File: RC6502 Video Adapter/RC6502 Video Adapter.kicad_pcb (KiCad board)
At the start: 2 copper layers, 99.1 x 66 mm, 19 parts, among them J1 CONN_01X39, J2 CONN_02X20, J3 Video, J4 FTDI, J5 ICSP, U1 ATMEGA328P-PU, Y1 16 Mhz

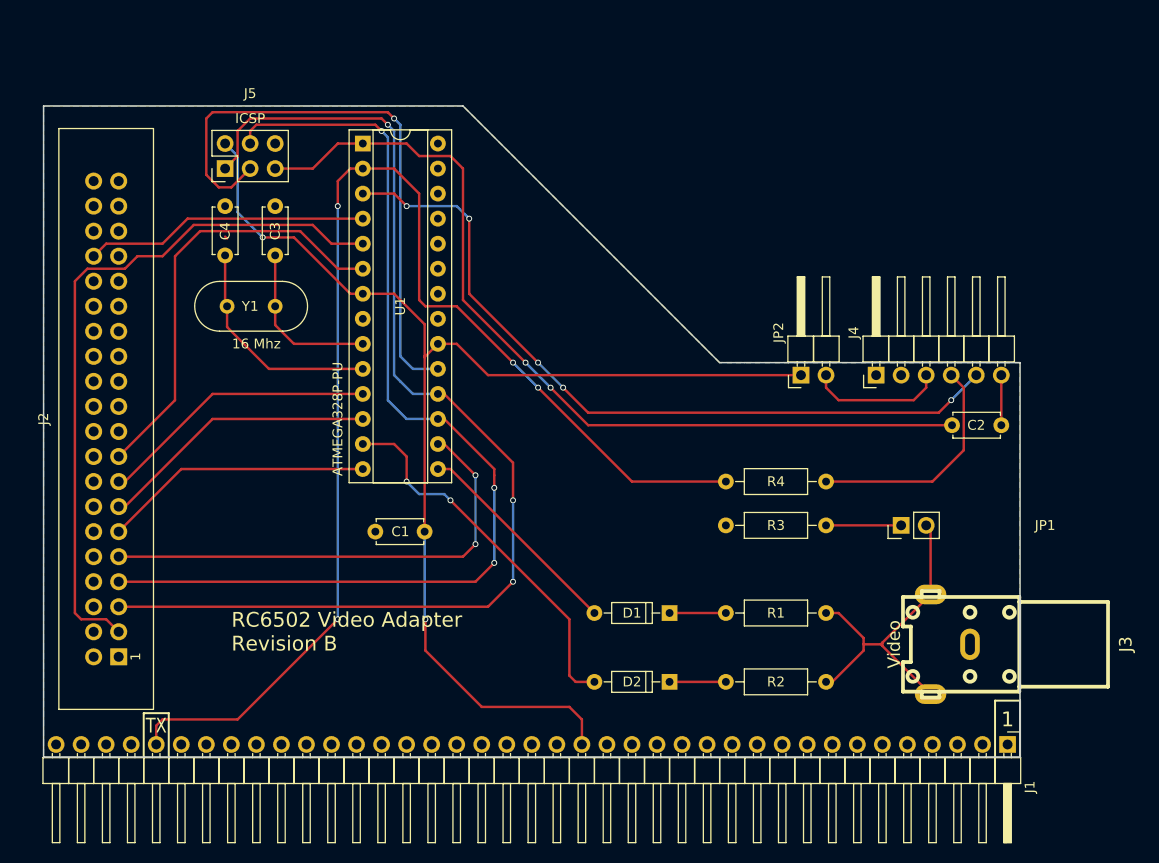
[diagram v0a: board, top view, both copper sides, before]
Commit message: Video Adapter revision B
Adds IO expanders for possibly offloading the actual image output rendering to an analog module via a separate connector.
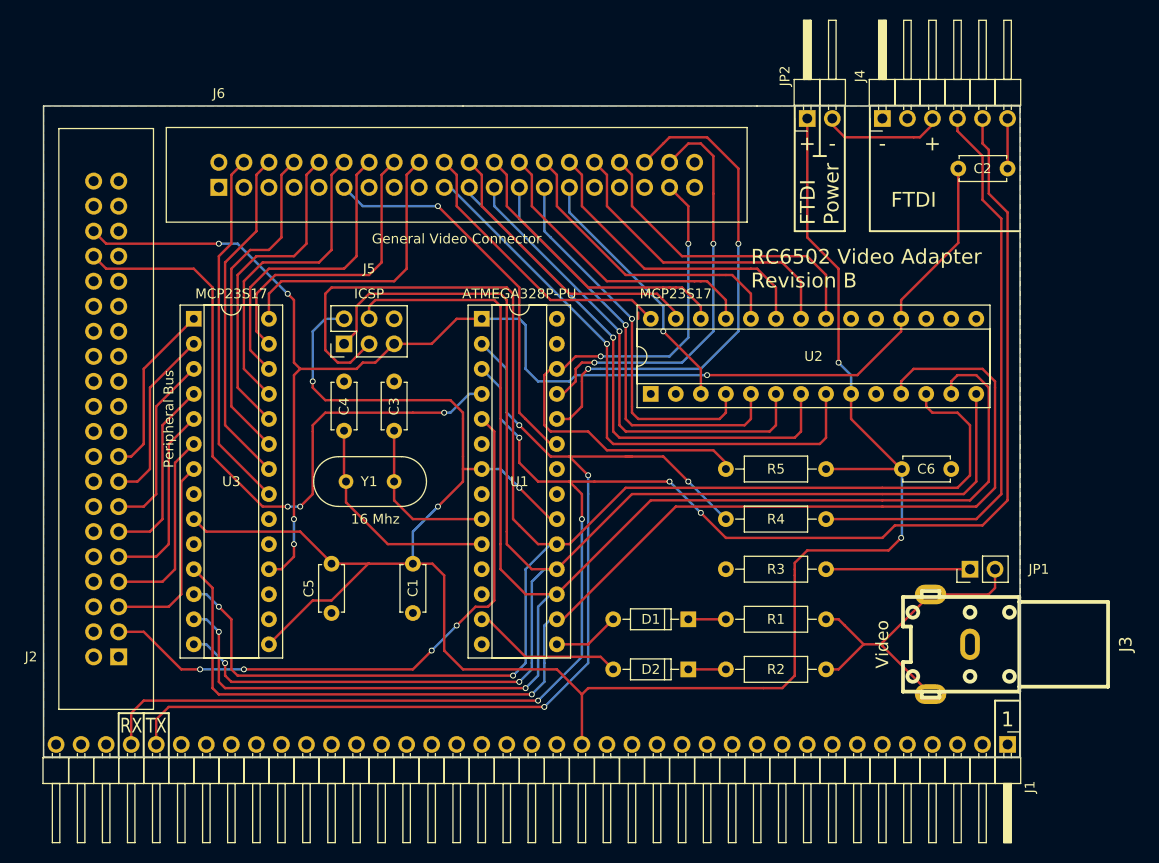
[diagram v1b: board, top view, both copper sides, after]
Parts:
- added C5: 100nF, Capacitors_THT:C_Disc_D4.7mm_W2.5mm_P5.00mm, F.Cu at (145.4, 132.7)
- added C6: 100nF, Capacitors_THT:C_Disc_D4.7mm_W2.5mm_P5.00mm, F.Cu at (208.3, 118.1)
- added J6: General Video Connector, Connectors:IDC_Header_Straight_40pins, F.Cu at (134.0, 89.5)
- added R5: 10k, Resistors_THT:R_Axial_DIN0207_L6.3mm_D2.5mm_P10.16mm_Horizontal, F.Cu at (185.4, 118.1)
- added U2: MCP23S17, Housings_DIP:DIP-28_W7.62mm_Socket, F.Cu at (177.8, 110.5)
- added U3: MCP23S17, Housings_DIP:DIP-28_W7.62mm_Socket, F.Cu at (131.4, 102.9)
- J2: value CONN_02X20 -> Peripheral Bus
- moved C2 26.0 mm to (214.0, 87.6)
- moved J4 26.0 mm to (201.3, 82.5)
- moved JP2 26.0 mm to (193.7, 82.5)
- moved C3 21.5 mm to (151.8, 109.2)
- moved C4 21.5 mm to (146.7, 109.2)
- moved J5 21.5 mm to (146.7, 105.4)
- moved U1 21.5 mm to (160.7, 102.9)
- moved Y1 21.5 mm to (151.8, 119.4)
- moved C1 9.09 mm to (153.7, 132.7), turned to 90 degrees
- moved JP1 8.28 mm to (210.2, 128.3)
- moved R3 4.45 mm to (185.4, 128.3)
- moved R4 3.81 mm to (195.6, 123.2)
- moved D2 2.29 mm to (181.6, 138.4)
- moved D1 2.01 mm to (181.6, 133.3)
- moved R2 1.27 mm to (195.6, 138.4)
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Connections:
- net Net-(J5-Pad3) renamed SCK
- C2 pad 2: RESET -> P_RESET
- J1 pad 36: (no net) -> RX
- J2 pad 36: (no net) -> P_RESET
- J4 pad 5: Net-(J4-Pad5) -> RX
- J5 pad 1: OUT_D6 -> MISO
- J5 pad 4: OUT_D5 -> MOSI
- J5 pad 5: RESET -> P_RESET
- U1 pad 1: RESET -> P_RESET
- U1 pad 11: OUT_D1 -> (no net)
- U1 pad 12: OUT_D2 -> (no net)
- U1 pad 14: OUT_D3 -> (no net)
- U1 pad 16: OUT_D4 -> SS
- U1 pad 17: OUT_D5 -> MOSI
- U1 pad 18: OUT_D6 -> MISO
- U1 pad 23: (no net) -> GV_CS
- U1 pad 24: (no net) -> GV_RW
- U1 pad 25: (no net) -> GV_E
- U1 pad 26: (no net) -> GV_DETECT
- U1 pad 3: Net-(J4-Pad5) -> RX
- U1 pad 6: OUT_D0 -> (no net)
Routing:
- net RX: track 0.00 -> 174.7 mm, vias 0 -> 5
- net MOSI: track 0.00 -> 163.2 mm, vias 0 -> 2
- net MISO: track 0.00 -> 155.5 mm, vias 0 -> 2
- net P_RESET: track 0.00 -> 142.2 mm, vias 0 -> 5
- net SS: track 0.00 -> 127.8 mm, vias 0 -> 1
- net SCK: track 59.8 -> 170.8 mm, vias 1 -> 2
- net VCC: track 125.8 -> 224.7 mm, vias 2 -> 5
- net OUT_D6: track 114.9 -> 20.1 mm, vias 3 -> 0
- net RESET: track 89.4 -> 0.00 mm, vias 2 -> 0
- net OUT_D5: track 104.8 -> 19.7 mm, vias 3 -> 0
- net Net-(J4-Pad5): track 77.5 -> 0.00 mm, vias 5 -> 0
- net GV_A8: track 0.00 -> 59.8 mm, vias 0 -> 1
- net GV_DETECT: track 0.00 -> 58.6 mm, vias 0 -> 2
- net GV_A9: track 0.00 -> 54.2 mm, vias 0 -> 1
- net GV_RW: track 0.00 -> 52.4 mm, vias 0 -> 2
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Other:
- outline, holes or cut-outs redrawn
- board text added: "+"
- board text added: "-"
- board text added: "FTDI"
- board text added: "FTDI Power"
- board text added: "RX"

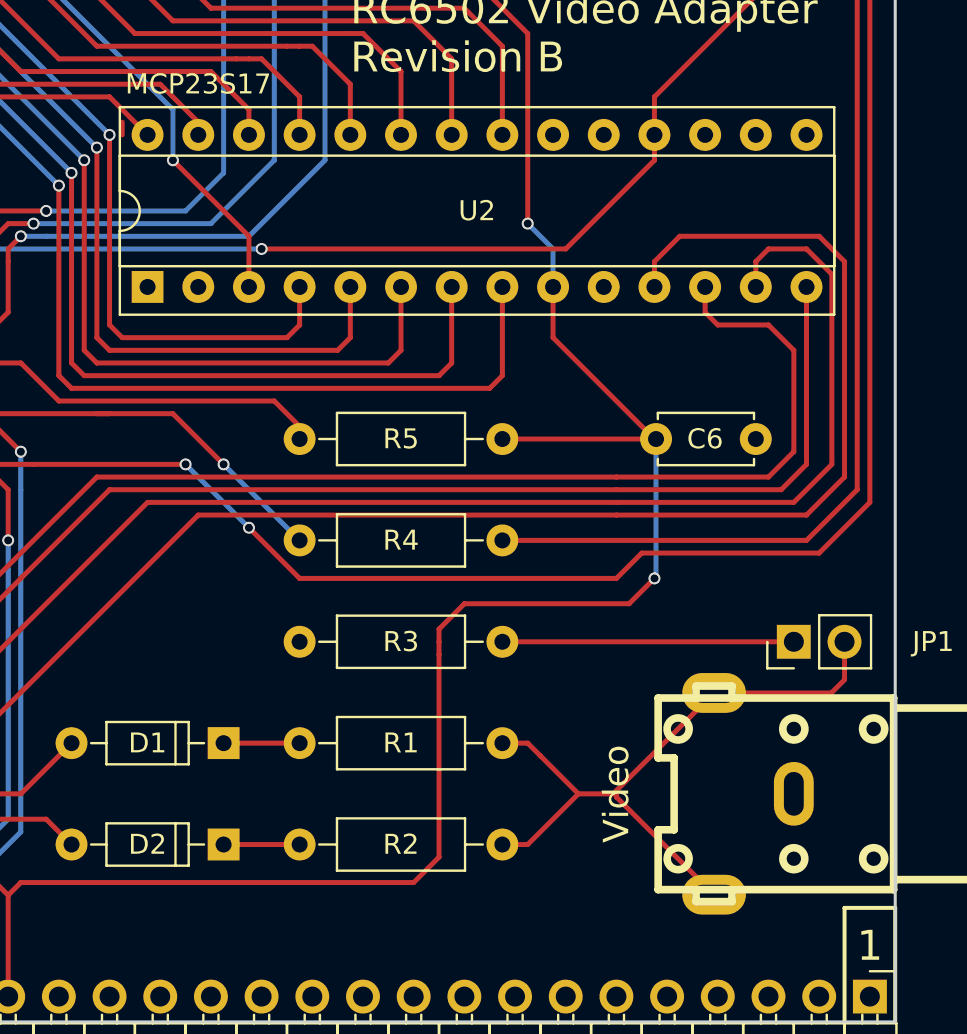
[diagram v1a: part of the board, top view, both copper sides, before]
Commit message: Fixed video adapter rca connector footprint.
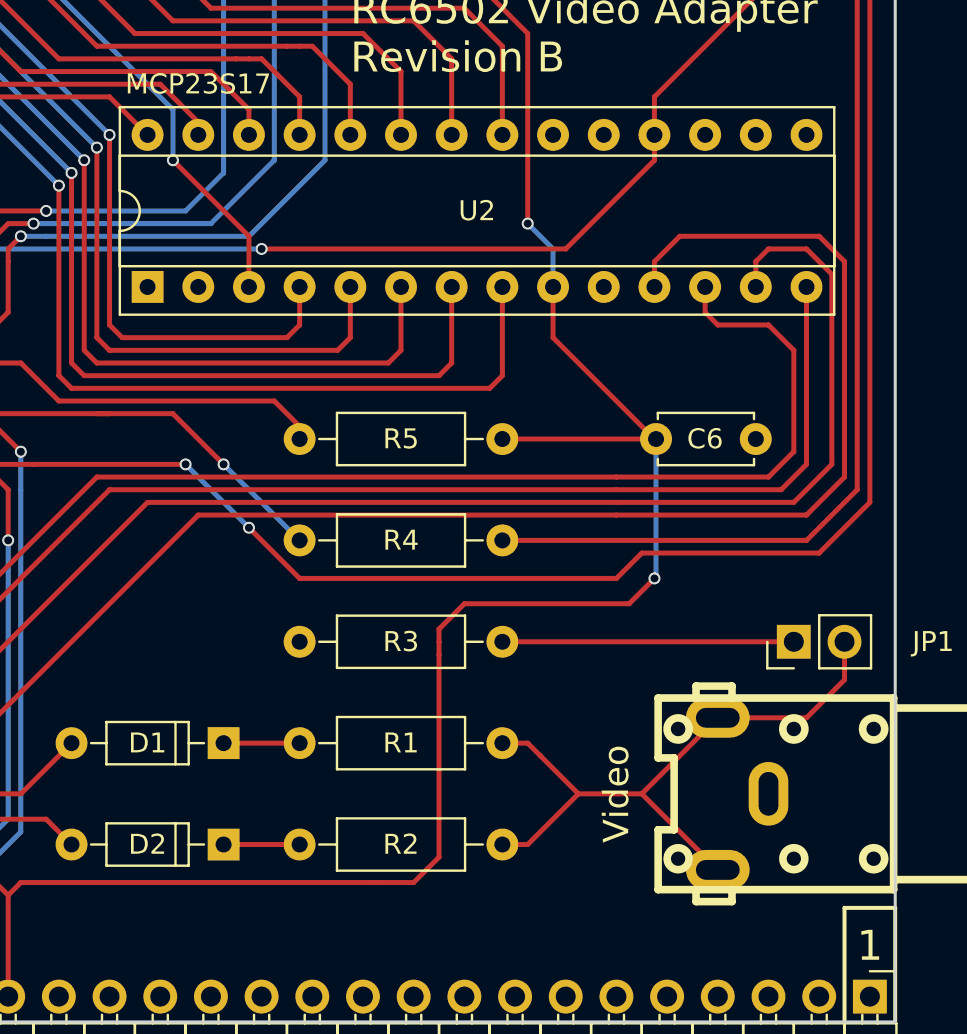
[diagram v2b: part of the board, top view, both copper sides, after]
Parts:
- J3: footprint w_conn_av:rca_yellow -> rca:rca_yellow
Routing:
- net Net-(J3-Pad2): track 34.6 -> 32.7 mm
- net (no net): track 0.64 -> 0.00 mm
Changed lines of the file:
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@@
     (thickness 1.6)
     (drawings 31)
-    (tracks 600)
+    (tracks 598)
     (zones 0)
     (modules 25)
@@
     (34 B.Paste user)
     (35 F.Paste user)
-    (36 B.SilkS user)
+    (36 B.SilkS user hide)
     (37 F.SilkS user)
     (38 B.Mask user)
@@
       (net 1 GND))
   )
-  (module w_conn_av:rca_yellow (layer F.Cu)
-    (at 210.185 135.89 90)
-    (descr "RCA Audio connector, yellow, Pro Signal p/n PSG01547")
-    (tags "rca, audio")
-    (fp_text reference J3 (at 0 15.7988 90) (layer F.SilkS)
-      (effects (font (thickness 0.3048)))
-    )
-    (fp_text value Video (at 0 -8.89 90) (layer F.SilkS)
-      (effects (font (thickness 0.3048)))
-    )
-    (fp_circle (center -3.2512 -5.79882) (end -3.79984 -5.79882) (layer F.SilkS) (width 0.381))
-    (fp_circle (center 3.2512 -5.79882) (end 2.70002 -5.84962) (layer F.SilkS) (width 0.381))
-    (fp_circle (center 3.2512 4.0005) (end 2.70002 4.04876) (layer F.SilkS) (width 0.381))
-    (fp_circle (center -3.2512 4.0005) (end -3.79984 3.9497) (layer F.SilkS) (width 0.381))
-    (fp_circle (center -3.2512 0) (end -3.79984 0) (layer F.SilkS) (width 0.381))
-    (fp_circle (center 3.2512 0) (end 2.70002 -0.0508) (layer F.SilkS) (width 0.381))
-    (fp_line (start -4.30022 5.00126) (end -4.30022 14.00048) (layer F.SilkS) (width 0.381))
-    (fp_line (start -4.30022 14.00048) (end 4.30022 14.00048) (layer F.SilkS) (width 0.381))
-    (fp_line (start 4.30022 14.00048) (end 4.30022 5.00126) (layer F.SilkS) (width 0.381))
-    (fp_line (start 4.8006 -4.89966) (end 5.40004 -4.89966) (layer F.SilkS) (width 0.381))
-    (fp_line (start 5.40004 -4.89966) (end 5.40004 -3.0988) (layer F.SilkS) (width 0.381))
-    (fp_line (start 5.40004 -3.0988) (end 4.8006 -3.0988) (layer F.SilkS) (width 0.381))
-    (fp_line (start -5.40004 -4.89966) (end -4.8006 -4.89966) (layer F.SilkS) (width 0.381))
-    (fp_line (start -4.8006 -3.0988) (end -5.40004 -3.0988) (layer F.SilkS) (width 0.381))
-    (fp_line (start -5.40004 -3.0988) (end -5.40004 -4.89966) (layer F.SilkS) (width 0.381))
-    (fp_line (start -4.8006 -6.79958) (end -1.80086 -6.79958) (layer F.SilkS) (width 0.381))
-    (fp_line (start -1.80086 -6.79958) (end -1.80086 -5.99948) (layer F.SilkS) (width 0.381))
-    (fp_line (start -1.80086 -5.99948) (end 1.80086 -5.99948) (layer F.SilkS) (width 0.381))
-    (fp_line (start 1.80086 -5.99948) (end 1.80086 -6.79958) (layer F.SilkS) (width 0.381))
-    (fp_line (start 1.80086 -6.79958) (end 4.8006 -6.79958) (layer F.SilkS) (width 0.381))
-    (fp_line (start 4.8006 5.00126) (end -4.8006 5.00126) (layer F.SilkS) (width 0.381))
-    (fp_line (start -4.8006 4.99872) (end -4.8006 -6.80212) (layer F.SilkS) (width 0.381))
-    (fp_line (start 4.8006 -6.79958) (end 4.8006 5.00126) (layer F.SilkS) (width 0.381))
-    (pad 2 thru_hole oval (at 5.0546 -3.99796 90) (size 1.99898 3.19786) (drill oval 0.99568 2.1971) (layers *.Cu *.Mask F.SilkS)
-      (net 15 "Net-(J3-Pad2)"))
-    (pad 1 thru_hole oval (at 0 0 90) (size 3.19786 1.99898) (drill oval 2.1971 0.99568) (layers *.Cu *.Mask F.SilkS)
-      (net 1 GND))
-    (pad 2 thru_hole oval (at -5.0546 -3.99796 90) (size 1.99898 3.19786) (drill oval 0.99568 2.1971) (layers *.Cu *.Mask F.SilkS)
-      (net 15 "Net-(J3-Pad2)"))
-    (model walter/conn_av/rca_yellow.wrl
-      (at (xyz 0 0 0))
-      (scale (xyz 1 1 1))
-      (rotate (xyz 0 0 0))
-    )
-  )
   (module Pin_Headers:Pin_Header_Angled_1x06_Pitch2.54mm (layer F.Cu)
     (at 201.295 82.55 90)
@@
     )
   )
+  (module rca:rca_yellow (layer F.Cu)
+    (at 210.185 135.89 90)
+    (descr "RCA Audio connector, yellow, Pro Signal p/n PSG01547")
+    (tags "rca, audio")
+    (fp_text reference J3 (at 0 15.7988 90) (layer F.SilkS)
+      (effects (font (thickness 0.3048)))
+    )
+    (fp_text value Video (at 0 -8.89 90) (layer F.SilkS)
+      (effects (font (thickness 0.3048)))
+    )
+    (fp_circle (center -3.2512 -5.79882) (end -3.79984 -5.79882) (layer F.SilkS) (width 0.381))
+    (fp_circle (center 3.2512 -5.79882) (end 2.70002 -5.84962) (layer F.SilkS) (width 0.381))
+    (fp_circle (center 3.2512 4.0005) (end 2.70002 4.04876) (layer F.SilkS) (width 0.381))
+    (fp_circle (center -3.2512 4.0005) (end -3.79984 3.9497) (layer F.SilkS) (width 0.381))
+    (fp_circle (center -3.2512 0) (end -3.79984 0) (layer F.SilkS) (width 0.381))
+    (fp_circle (center 3.2512 0) (end 2.70002 -0.0508) (layer F.SilkS) (width 0.381))
+    (fp_line (start -4.30022 5.00126) (end -4.30022 14.00048) (layer F.SilkS) (width 0.381))
+    (fp_line (start -4.30022 14.00048) (end 4.30022 14.00048) (layer F.SilkS) (width 0.381))
+    (fp_line (start 4.30022 14.00048) (end 4.30022 5.00126) (layer F.SilkS) (width 0.381))
+    (fp_line (start 4.8006 -4.89966) (end 5.40004 -4.89966) (layer F.SilkS) (width 0.381))
+    (fp_line (start 5.40004 -4.89966) (end 5.40004 -3.0988) (layer F.SilkS) (width 0.381))
+    (fp_line (start 5.40004 -3.0988) (end 4.8006 -3.0988) (layer F.SilkS) (width 0.381))
+    (fp_line (start -5.40004 -4.89966) (end -4.8006 -4.89966) (layer F.SilkS) (width 0.381))
+    (fp_line (start -4.8006 -3.0988) (end -5.40004 -3.0988) (layer F.SilkS) (width 0.381))
+    (fp_line (start -5.40004 -3.0988) (end -5.40004 -4.89966) (layer F.SilkS) (width 0.381))
+    (fp_line (start -4.8006 -6.79958) (end -1.80086 -6.79958) (layer F.SilkS) (width 0.381))
+    (fp_line (start -1.80086 -6.79958) (end -1.80086 -5.99948) (layer F.SilkS) (width 0.381))
+    (fp_line (start -1.80086 -5.99948) (end 1.80086 -5.99948) (layer F.SilkS) (width 0.381))
+    (fp_line (start 1.80086 -5.99948) (end 1.80086 -6.79958) (layer F.SilkS) (width 0.381))
+    (fp_line (start 1.80086 -6.79958) (end 4.8006 -6.79958) (layer F.SilkS) (width 0.381))
+    (fp_line (start 4.8006 5.00126) (end -4.8006 5.00126) (layer F.SilkS) (width 0.381))
+    (fp_line (start -4.8006 4.99872) (end -4.8006 -6.80212) (layer F.SilkS) (width 0.381))
+    (fp_line (start 4.8006 -6.79958) (end 4.8006 5.00126) (layer F.SilkS) (width 0.381))
+    (pad 2 thru_hole oval (at 3.81 -3.81 90) (size 1.99898 3.19786) (drill oval 0.99568 2.1971) (layers *.Cu *.Mask F.SilkS)
+      (net 15 "Net-(J3-Pad2)"))
+    (pad 1 thru_hole oval (at 0 -1.27 90) (size 3.19786 1.99898) (drill oval 2.1971 0.99568) (layers *.Cu *.Mask F.SilkS)
+      (net 1 GND))
+    (pad 2 thru_hole oval (at -3.81 -3.81 90) (size 1.99898 3.19786) (drill oval 0.99568 2.1971) (layers *.Cu *.Mask F.SilkS)
+      (net 15 "Net-(J3-Pad2)"))
+    (model walter/conn_av/rca_yellow.wrl
+      (at (xyz 0 0 0))
+      (scale (xyz 1 1 1))
+      (rotate (xyz 0 0 0))
+    )
+  )
   (gr_text + (at 206.375 85.09) (layer F.SilkS)
     (effects (font (size 1.5 1.5) (thickness 0.3)))
@@
   (gr_line (start 116.205 81.28) (end 116.205 147.32) (angle 90) (layer Edge.Cuts) (width 0.15))
   (gr_line (start 215.265 147.32) (end 116.205 147.32) (angle 90) (layer Edge.Cuts) (width 0.15))
-  (segment (start 176.53 102.235) (end 176.53 102.87) (width 0.25) (layer F.Cu) (net 0))
   (segment (start 143.51 109.855) (end 144.78 111.125) (width 0.25) (layer F.Cu) (net 2))
   (segment (start 158.75 112.395) (end 158.75 113.03) (width 0.25) (layer F.Cu) (net 2))
@@
   (segment (start 196.215 83.185) (end 196.215 82.55) (width 0.25) (layer F.Cu) (net 13))
   (segment (start 210.185 128.27) (end 195.58 128.27) (width 0.25) (layer F.Cu) (net 14))
-  (segment (start 206.18704 130.8354) (end 212.0646 130.8354) (width 0.25) (layer F.Cu) (net 15))
+  (segment (start 206.375 132.08) (end 210.82 132.08) (width 0.25) (layer F.Cu) (net 15))
   (segment (start 212.725 130.175) (end 212.725 128.27) (width 0.25) (layer F.Cu) (net 15))
-  (segment (start 212.0646 130.8354) (end 212.725 130.175) (width 0.25) (layer F.Cu) (net 15))
+  (segment (start 210.82 132.08) (end 212.725 130.175) (width 0.25) (layer F.Cu) (net 15))
+  (segment (start 202.565 135.89) (end 206.375 139.7) (width 0.25) (layer F.Cu) (net 15))
+  (segment (start 201.13244 135.89) (end 202.565 135.89) (width 0.25) (layer F.Cu) (net 15))
+  (segment (start 199.39 135.89) (end 201.13244 135.89) (width 0.25) (layer F.Cu) (net 15))
+  (segment (start 202.565 135.89) (end 206.375 132.08) (width 0.25) (layer F.Cu) (net 15))
   (segment (start 197.485 133.985) (end 196.85 133.35) (width 0.25) (layer F.Cu) (net 15))
   (segment (start 199.39 135.89) (end 197.485 133.985) (width 0.25) (layer F.Cu) (net 15))
@@
   (segment (start 195.58 138.43) (end 196.85 138.43) (width 0.25) (layer F.Cu) (net 15))
   (segment (start 196.85 138.43) (end 199.39 135.89) (width 0.25) (layer F.Cu) (net 15))
-  (segment (start 201.295 135.72744) (end 201.295 136.05256) (width 0.25) (layer F.Cu) (net 15))
-  (segment (start 201.295 136.05256) (end 206.18704 140.9446) (width 0.25) (layer F.Cu) (net 15))
-  (segment (start 199.39 135.89) (end 201.13244 135.89) (width 0.25) (layer F.Cu) (net 15))
-  (segment (start 201.13244 135.89) (end 201.295 135.72744) (width 0.25) (layer F.Cu) (net 15))
-  (segment (start 201.295 135.72744) (end 206.18704 130.8354) (width 0.25) (layer F.Cu) (net 15))
   (segment (start 208.915 82.55) (end 208.915 83.82) (width 0.25) (layer F.Cu) (net 16))
   (segment (start 211.455 90.805) (end 213.36 92.71) (width 0.25) (layer F.Cu) (net 16))
